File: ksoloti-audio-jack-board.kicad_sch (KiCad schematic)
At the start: 18 parts, among them J1 LINE_IN_OUT, J10 OUT_L_VOL, J11 OUT_R_VOL, J12 HP_VOL, J2 HP_OUT, J3 IN_L, J4 IN_R, J5 OUT_L, J6 OUT_R, J7 HP_OUT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

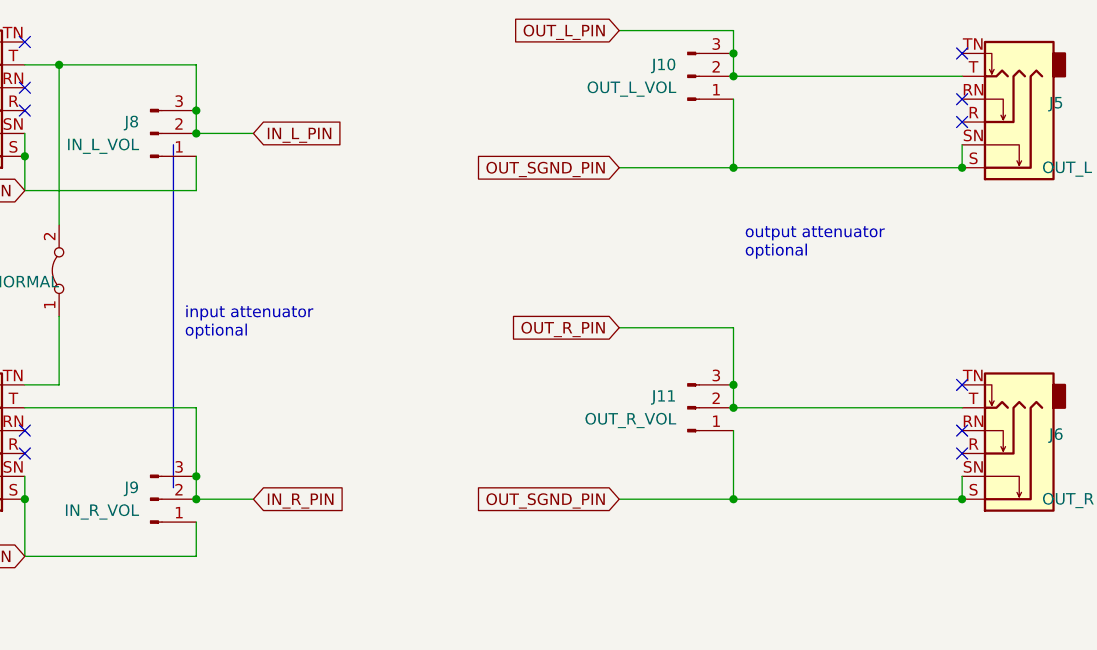
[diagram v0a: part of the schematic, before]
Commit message: update project (board dimensions now 100m*34mm)
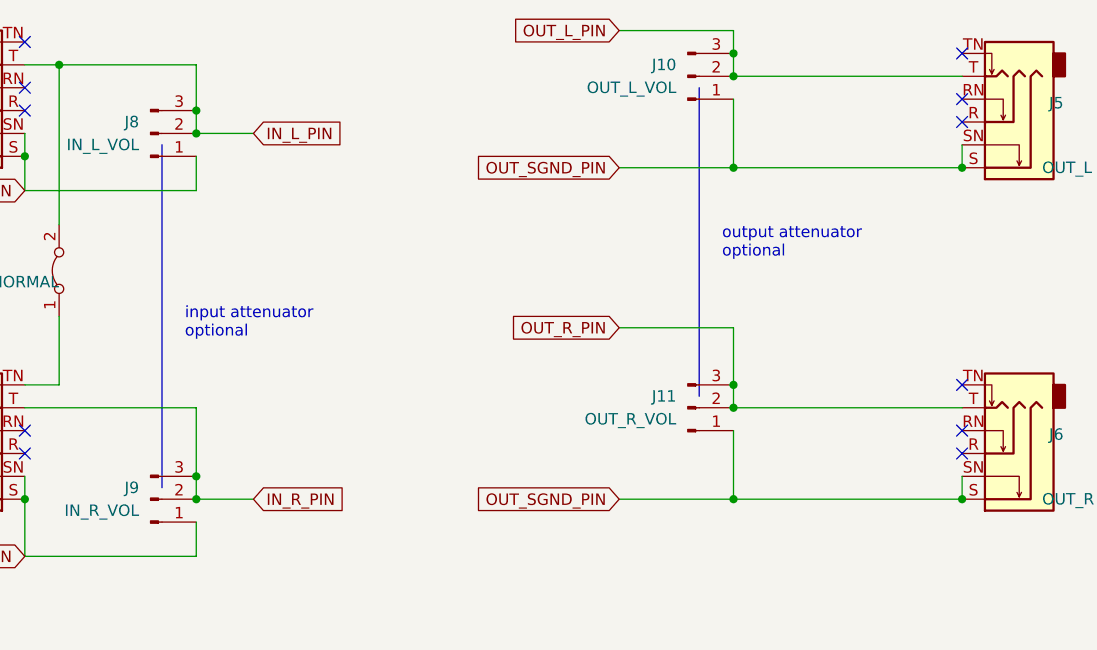
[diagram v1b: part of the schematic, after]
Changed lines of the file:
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@@
+    (stroke (width 0) (type default) (color 0 0 0 0))
+  )
+  (polyline (pts (xy 204.47 72.39) (xy 204.47 106.68))
     (stroke (width 0) (type default) (color 0 0 0 0))
   )
@@
     (stroke (width 0) (type default) (color 0 0 0 0))
   )
-  (polyline (pts (xy 146.05 78.74) (xy 146.05 116.84))
+  (polyline (pts (xy 144.78 78.74) (xy 144.78 116.84))
     (stroke (width 0) (type default) (color 0 0 0 0))
   )
@@
     (effects (font (size 1.27 1.27)) (justify left bottom))
   )
-  (text "output attenuator\noptional" (at 209.55 91.44 0)
+  (text "output attenuator\noptional" (at 207.01 91.44 0)
     (effects (font (size 1.27 1.27)) (justify left bottom))
   )
